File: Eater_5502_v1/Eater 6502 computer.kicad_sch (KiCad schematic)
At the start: 99 parts, among them J1 DE9_Plug, J2 PA_CONN, J3 PB_CONN, J4 ADDR_LOW, J5 DATA_CONN, J6 CPU_CONN, J7 CS_CONN, J8 PWR_IN, J9 ADDR_HIGH, SW1 RESET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

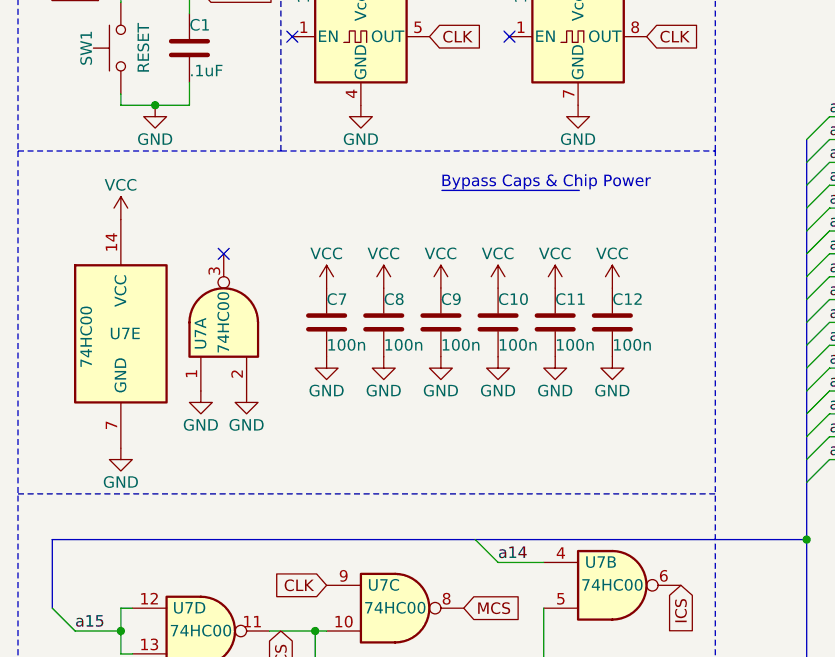
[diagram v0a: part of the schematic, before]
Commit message: updated board design to include bigger capacitor footprints, added the bulk decoupling cap to the power input, and made text larger in places to improve readability
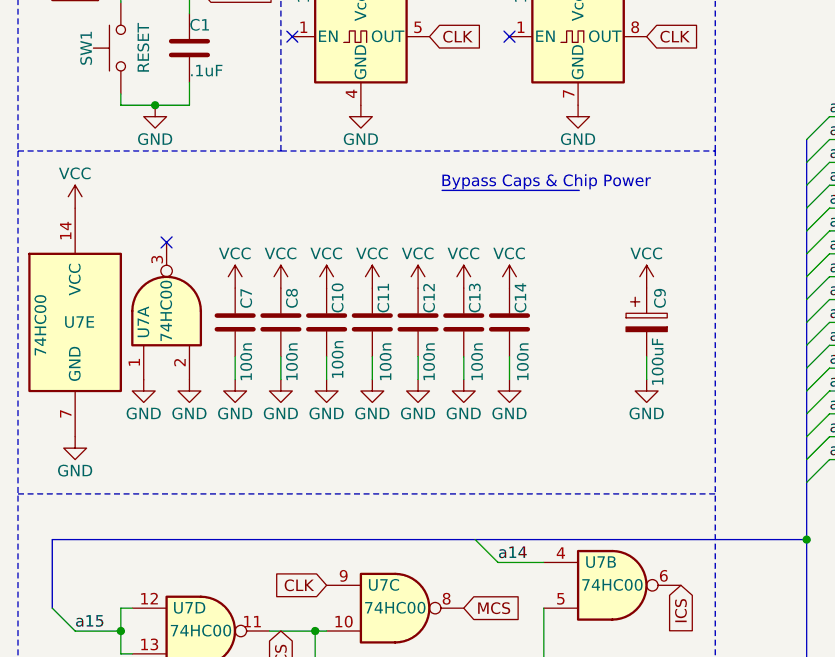
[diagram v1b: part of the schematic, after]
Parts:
- removed C9: 100n, Capacitor_THT:C_Disc_D5.0mm_W2.5mm_P2.50mm, symbol Device:C
- added C13, C14: 100n, Capacitor_THT:C_Disc_D5.0mm_W2.5mm_P5.00mm, symbol Device:C
- added C9: 100uF, Capacitor_THT:CP_Radial_D5.0mm_P2.00mm, symbol Device:C_Polarized
- C1, C10, C11, C12, C3, C4, C5, C6, C7, C8: footprint Capacitor_THT:C_Disc_D5.0mm_W2.5mm_P2.50mm -> Capacitor_THT:C_Disc_D5.0mm_W2.5mm_P5.00mm
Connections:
- net GND: now also C13.2, C14.2, C9.2
- net VCC: now also C13.1, C14.1, C9.1
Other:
- moved on the sheet: C10, C11, C12, C7, C8, U7A, U7E
